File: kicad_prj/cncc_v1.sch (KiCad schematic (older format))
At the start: 0 parts

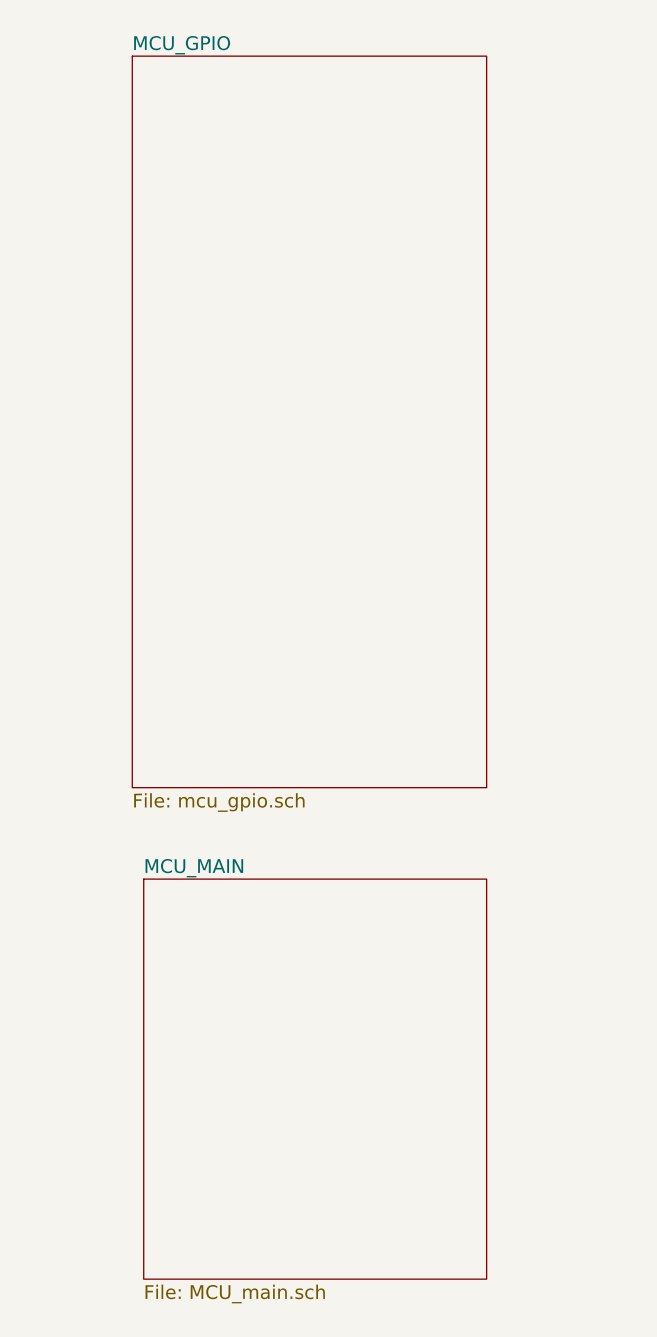
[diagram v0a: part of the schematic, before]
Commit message: Ethernet and decoupling capacitors
Change ethernet jack symbol to add LEDs.
Change all sheets to have power inputs tied to a global label instead of
sheet pins.
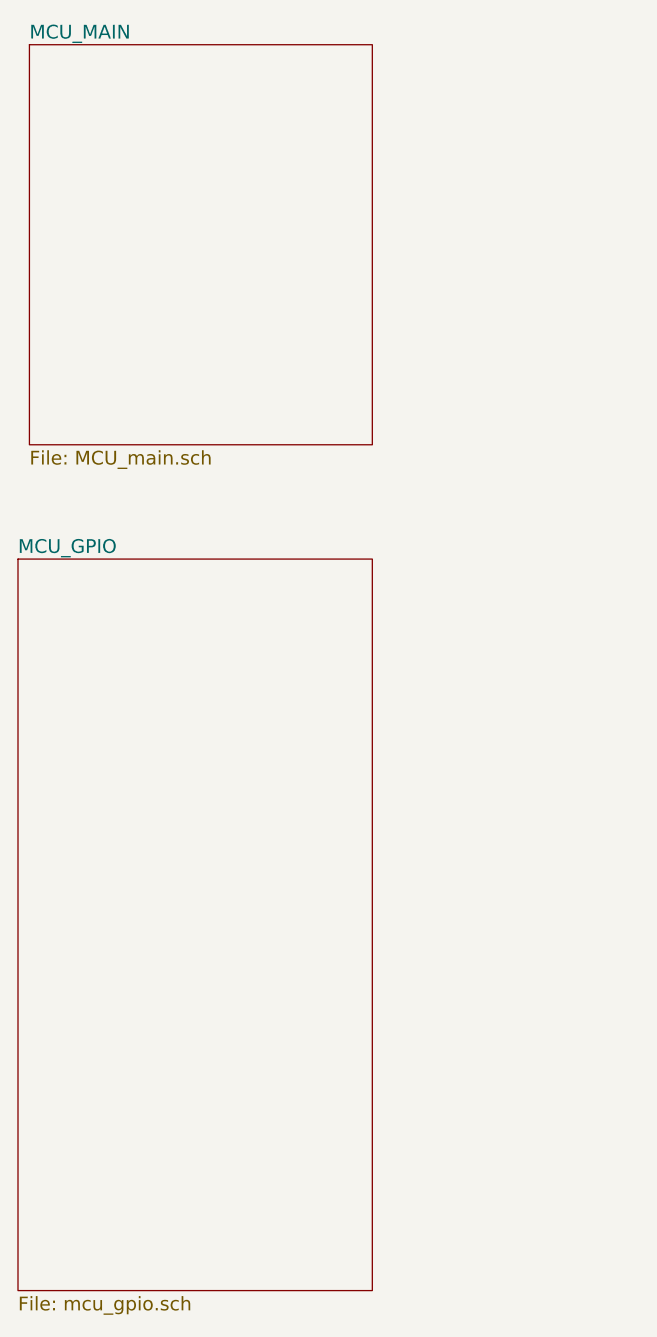
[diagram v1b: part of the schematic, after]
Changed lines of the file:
@@
 EESchema Schematic File Version 2
+LIBS:cncc_v1-rescue
 LIBS:power
 LIBS:device
@@
 CH[0..3]
 $Sheet
-S 1750 1100 1550 3200
+S 1250 3300 1550 3200
 U 566CD168
 F0 "MCU_GPIO" 60
@@
 $EndSheet
 $Sheet
-S 1800 4700 1500 1750
+S 1300 1050 1500 1750
 U 566DECB3
 F0 "MCU_MAIN" 60
